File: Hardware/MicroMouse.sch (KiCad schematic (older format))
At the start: 70 parts, among them J1 TSW-106-25-S-S-RA, J3 PRPC040SFAN-RC (06), J4 B5B-XH-A(LF)(SN), J5 B5B-XH-A(LF)(SN), Q1 NXV75UPR, SW1 SPST, SW2 SPST, SW3 SPST, SW4 SPST, SW5 L101011MS02Q, SW6 SPST, SW7 SPST, SW8 SPST, U1 ADP1612, U2 PIC16F886-E_SO, U3 ULN2803ADW, U4 74LVC1G332GV-Q100H, U5 ADCMP393ARZ, U6 TCRT1000, U7 TCRT1000, U8 TCRT1000, Y1 32.768KHZ

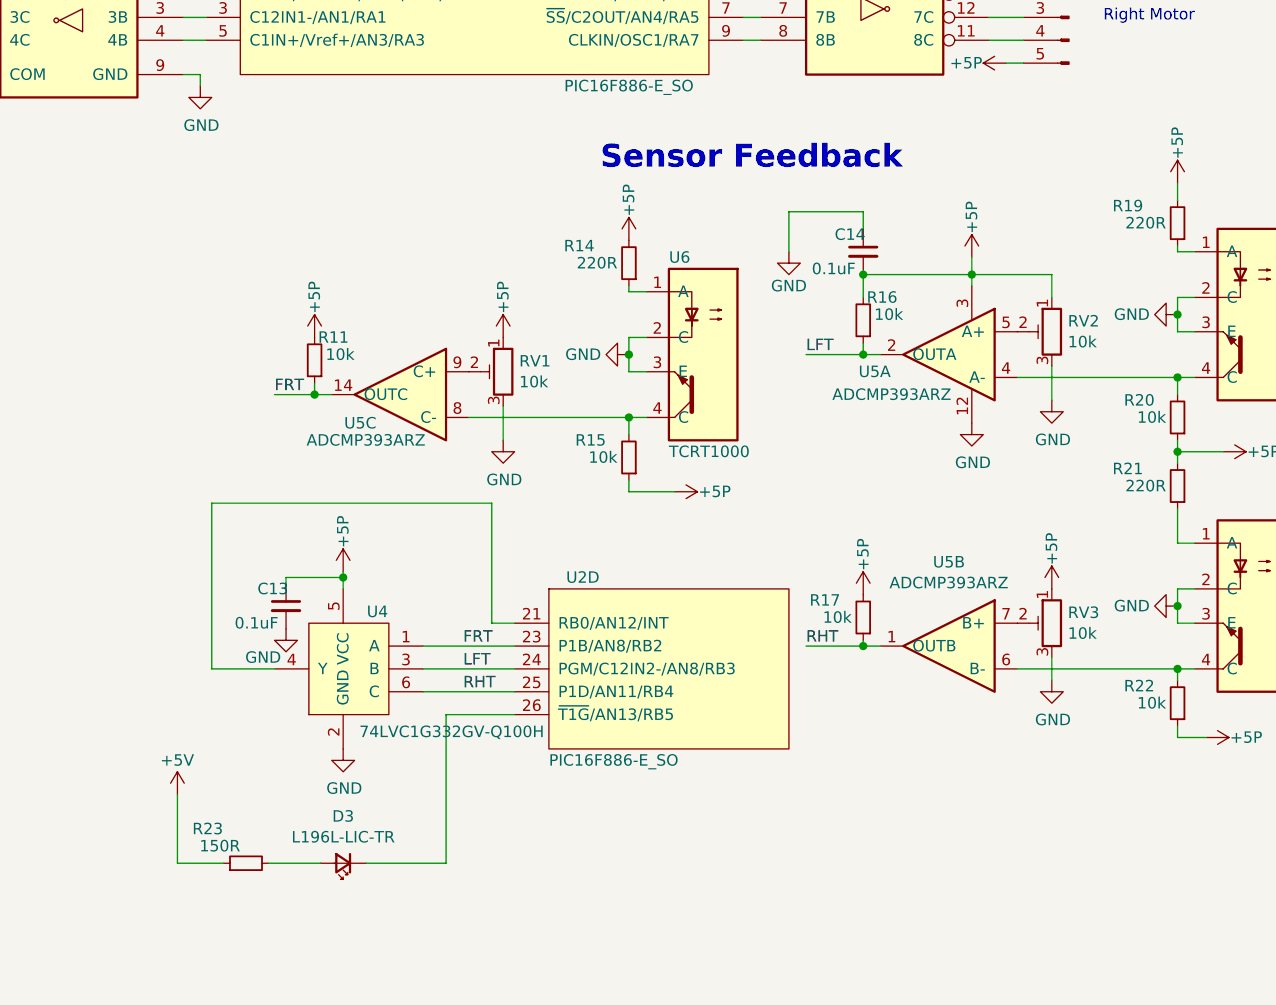
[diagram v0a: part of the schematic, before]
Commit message: Add LED for IR detection
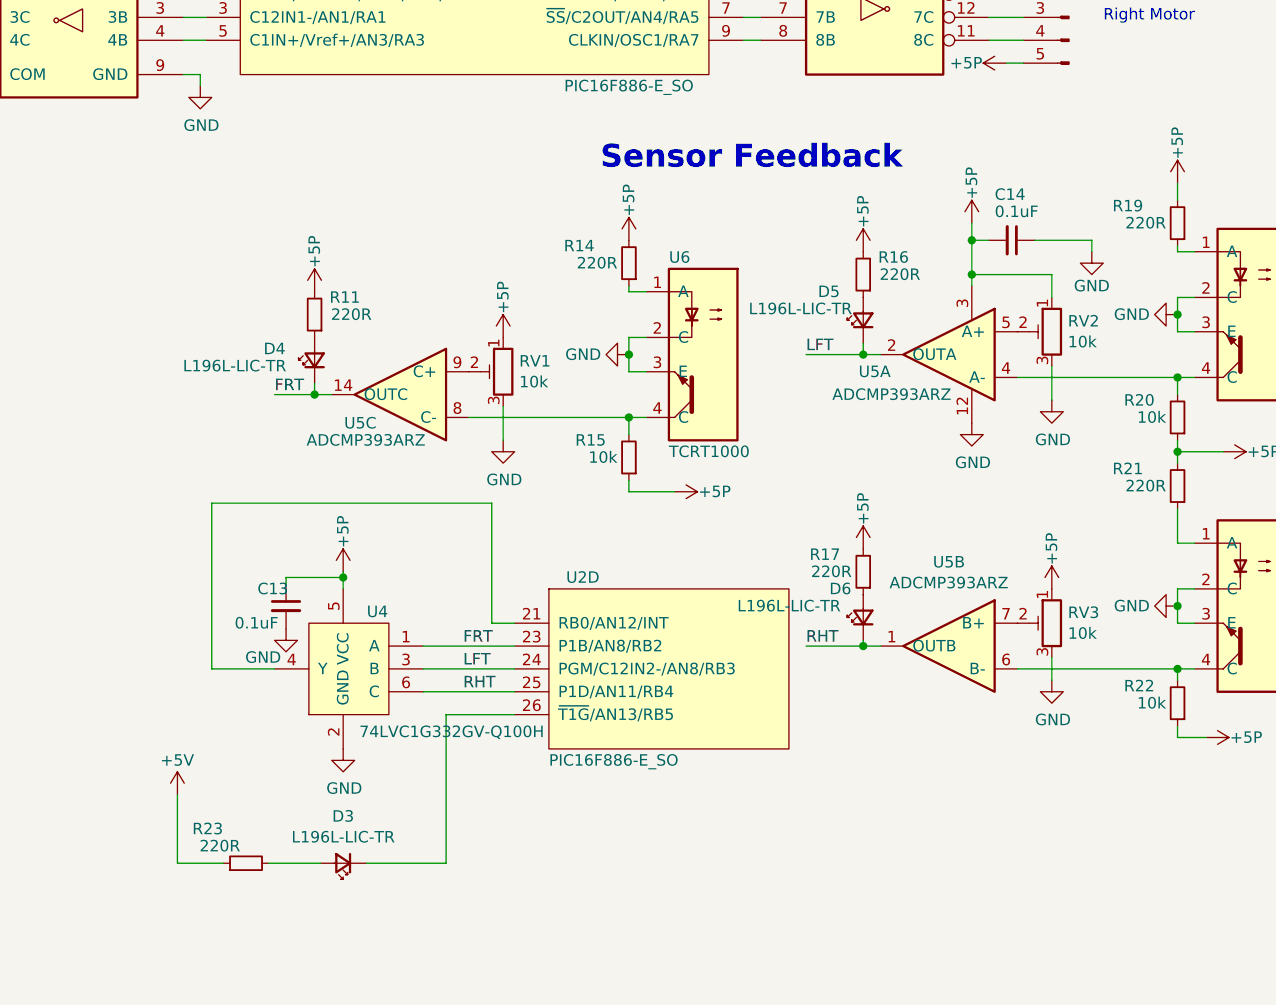
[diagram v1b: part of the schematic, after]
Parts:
- added D4, D5, D6: L196L-LIC-TR, Micro-Footprint:LTST-C170-0805, symbol Device:LED_Small
- R11, R16, R17: value 10k -> 220R
- R23: value 150R -> 220R
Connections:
- net FRT: now also D4.1 (K); no longer R11.1
- net LFT: now also D5.1 (K); no longer R16.1
- net RHT: now also D6.1 (K); no longer R17.1
- new net: D4.2 (A), R11.1
- new net: D5.2 (A), R16.1
- new net: D6.2 (A), R17.1
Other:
- moved on the sheet: C14, R11, R16, R17
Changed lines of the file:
@@
 EESchema Schematic File Version 4
-EELAYER 30 0
+LIBS:MicroMouse-cache
+EELAYER 29 0
 EELAYER END
 $Descr A4 11693 8268
@@
 Title "MicroMouse Mainboard with PIC16F886"
 Date "2021-04-11"
-Rev "1.00"
+Rev "1.10"
 Comp "KidoTech"
 Comment1 ""
@@
 L power:+5P #PWR037
 U 1 1 6090CAF6
-P 9200 4125
-F 0 "#PWR037" H 9200 3975 50  0001 C CNN
-F 1 "+5P" V 9200 4300 50  0000 C CNN
-F 2 "" H 9200 4125 50  0001 C CNN
-F 3 "" H 9200 4125 50  0001 C CNN
-	1    9200 4125
+P 9200 3975
+F 0 "#PWR037" H 9200 3825 50  0001 C CNN
+F 1 "+5P" V 9200 4150 50  0000 C CNN
+F 2 "" H 9200 3975 50  0001 C CNN
+F 3 "" H 9200 3975 50  0001 C CNN
+	1    9200 3975
 	1    0    0    -1
 $EndComp
@@
 L Device:R_Small R16
 U 1 1 60924A2D
-P 8725 4400
-F 0 "R16" H 8575 4300 50  0000 L CNN
-F 1 "10k" H 8550 4375 50  0000 L CNN
-F 2 "Micro-Footprint:RES0603" H 8725 4400 50  0001 C CNN
-F 3 "~" H 8725 4400 50  0001 C CNN
-	1    8725 4400
+P 8725 4200
+F 0 "R16" H 8525 4125 50  0000 L CNN
+F 1 "220R" H 8475 4200 50  0000 L CNN
+F 2 "Micro-Footprint:RES0603" H 8725 4200 50  0001 C CNN
+F 3 "~" H 8725 4200 50  0001 C CNN
+	1    8725 4200
 	-1   0    0    1
 $EndComp
@@
 Wire Wire Line
 	9200 4250 9200 4200
-Wire Wire Line
-	8725 4300 8725 4200
-Wire Wire Line
-	8725 4200 9200 4200
 Connection ~ 9200 4200
-Wire Wire Line
-	9200 4200 9200 4125
 $Comp
 L Device:C_Small C14
 U 1 1 60949563
-P 8725 4100
-F 0 "C14" H 8600 4175 50  0000 L CNN
-F 1 "0.1uF" H 8500 4025 50  0000 L CNN
-F 2 "Micro-Footprint:CAP0603" H 8725 4100 50  0001 C CNN
-F 3 "~" H 8725 4100 50  0001 C CNN
-	1    8725 4100
-	1    0    0    -1
+P 9375 4050
+F 0 "C14" V 9175 3975 50  0000 L CNN
+F 1 "0.1uF" V 9250 3975 50  0000 L CNN
+F 2 "Micro-Footprint:CAP0603" H 9375 4050 50  0001 C CNN
+F 3 "~" H 9375 4050 50  0001 C CNN
+	1    9375 4050
+	0    1    1    0
 $EndComp
 $Comp
 L power:GND #PWR035
 U 1 1 609636D6
-P 8400 4100
-F 0 "#PWR035" H 8400 3850 50  0001 C CNN
-F 1 "GND" H 8400 3950 50  0000 C CNN
-F 2 "" H 8400 4100 50  0001 C CNN
-F 3 "" H 8400 4100 50  0001 C CNN
-	1    8400 4100
+P 9725 4100
+F 0 "#PWR035" H 9725 3850 50  0001 C CNN
+F 1 "GND" H 9725 3950 50  0000 C CNN
+F 2 "" H 9725 4100 50  0001 C CNN
+F 3 "" H 9725 4100 50  0001 C CNN
+	1    9725 4100
 	1    0    0    -1
 $EndComp
@@
 L power:+5P #PWR036
 U 1 1 609B2C17
-P 8725 5600
-F 0 "#PWR036" H 8725 5450 50  0001 C CNN
-F 1 "+5P" V 8725 5775 50  0000 C CNN
-F 2 "" H 8725 5600 50  0001 C CNN
-F 3 "" H 8725 5600 50  0001 C CNN
-	1    8725 5600
+P 8725 5400
+F 0 "#PWR036" H 8725 5250 50  0001 C CNN
+F 1 "+5P" V 8725 5575 50  0000 C CNN
+F 2 "" H 8725 5400 50  0001 C CNN
+F 3 "" H 8725 5400 50  0001 C CNN
+	1    8725 5400
 	1    0    0    -1
 $EndComp
@@
 L Device:R_Small R17
 U 1 1 609A562F
-P 8725 5700
-F 0 "R17" H 8825 5625 50  0000 L CNN
-F 1 "10k" H 8775 5700 50  0000 L CNN
-F 2 "Micro-Footprint:RES0603" H 8725 5700 50  0001 C CNN
-F 3 "~" H 8725 5700 50  0001 C CNN
-	1    8725 5700
+P 8725 5500
+F 0 "R17" H 8825 5425 50  0000 L CNN
+F 1 "220R" H 8775 5500 50  0000 L CNN
+F 2 "Micro-Footprint:RES0603" H 8725 5500 50  0001 C CNN
+F 3 "~" H 8725 5500 50  0001 C CNN
+	1    8725 5500
 	-1   0    0    1
 $EndComp
@@
 L Device:R_Small R11
 U 1 1 609FA98A
-P 6325 4575
-F 0 "R11" H 6175 4475 50  0000 L CNN
-F 1 "10k" H 6150 4550 50  0000 L CNN
-F 2 "Micro-Footprint:RES0603" H 6325 4575 50  0001 C CNN
-F 3 "~" H 6325 4575 50  0001 C CNN
-	1    6325 4575
+P 6325 4375
+F 0 "R11" H 6125 4300 50  0000 L CNN
+F 1 "220R" H 6075 4375 50  0000 L CNN
+F 2 "Micro-Footprint:RES0603" H 6325 4375 50  0001 C CNN
+F 3 "~" H 6325 4375 50  0001 C CNN
+	1    6325 4375
 	-1   0    0    1
 $EndComp
@@
 L power:+5P #PWR025
 U 1 1 60AB88D8
-P 6325 4475
-F 0 "#PWR025" H 6325 4325 50  0001 C CNN
-F 1 "+5P" V 6325 4650 50  0000 C CNN
-F 2 "" H 6325 4475 50  0001 C CNN
-F 3 "" H 6325 4475 50  0001 C CNN
-	1    6325 4475
+P 6325 4275
+F 0 "#PWR025" H 6325 4125 50  0001 C CNN
+F 1 "+5P" V 6325 4450 50  0000 C CNN
+F 2 "" H 6325 4275 50  0001 C CNN
+F 3 "" H 6325 4275 50  0001 C CNN
+	1    6325 4275
 	1    0    0    -1
 $EndComp
@@
 	8725 4550 8475 4550
 Connection ~ 8725 4550
-Connection ~ 8725 4200
-Wire Wire Line
-	8400 4100 8400 3925
-Wire Wire Line
-	8400 3925 8725 3925
-Wire Wire Line
-	8725 3925 8725 4000
 Text Label 8475 5825 0    50   ~ 0
 RHT
@@
 P 6025 6775
 F 0 "R23" V 6175 6875 50  0000 L CNN
-F 1 "150R" V 6100 6800 50  0000 L CNN
+F 1 "220R" V 6100 6800 50  0000 L CNN
 F 2 "Micro-Footprint:RES0603" H 6025 6775 50  0001 C CNN
 F 3 "~" H 6025 6775 50  0001 C CNN
@@
 Text Label 4025 7000 0    50   ~ 0
 C3
+$Comp
+L Device:LED_Small D4
+U 1 1 6073DD47
+P 6325 4575
+F 0 "D4" V 6375 4750 50  0000 C CNN
+F 1 "L196L-LIC-TR" V 6300 4925 50  0000 C CNN
+F 2 "Micro-Footprint:LTST-C170-0805" V 6325 4575 50  0001 C CNN
+F 3 "~" V 6325 4575 50  0001 C CNN
+	1    6325 4575
+	0    -1   -1   0
+$EndComp
+$Comp
+L Device:LED_Small D5
+U 1 1 6073EA1A
+P 8725 4400
+F 0 "D5" V 8850 4550 50  0000 C CNN
+F 1 "L196L-LIC-TR" V 8775 4675 50  0000 C CNN
+F 2 "Micro-Footprint:LTST-C170-0805" V 8725 4400 50  0001 C CNN
+F 3 "~" V 8725 4400 50  0001 C CNN
+	1    8725 4400
+	0    -1   -1   0
+$EndComp
+$Comp
+L Device:LED_Small D6
+U 1 1 6073EDC0
+P 8725 5700
+F 0 "D6" V 8850 5800 50  0000 C CNN
+F 1 "L196L-LIC-TR" V 8775 6025 50  0000 C CNN
+F 2 "Micro-Footprint:LTST-C170-0805" V 8725 5700 50  0001 C CNN
+F 3 "~" V 8725 5700 50  0001 C CNN
+	1    8725 5700
+	0    -1   -1   0
+$EndComp
+Wire Wire Line
+	9200 3975 9200 4050
+Wire Wire Line
+	9275 4050 9200 4050
+Connection ~ 9200 4050
+Wire Wire Line
+	9200 4050 9200 4200
+Wire Wire Line
+	9475 4050 9725 4050
+Wire Wire Line
+	9725 4050 9725 4100
+$Comp
+L power:+5P #PWR049
+U 1 1 607CD14E
+P 8725 4100
+F 0 "#PWR049" H 8725 3950 50  0001 C CNN
+F 1 "+5P" V 8725 4275 50  0000 C CNN
+F 2 "" H 8725 4100 50  0001 C CNN
+F 3 "" H 8725 4100 50  0001 C CNN
+	1    8725 4100
+	1    0    0    -1
+$EndComp
 $EndSCHEMATC

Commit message: Update Layout
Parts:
- removed BT1: 1042, Micro-Footprint:1042-SMD, symbol Device:Battery_Cell
- removed J3: PRPC040SFAN-RC (06), Micro-Footprint:THRU-254-STR-6P, symbol Connector:Conn_01x06_Male
- removed SW5: L101011MS02Q, Micro-Footprint:L101011-THRU, symbol Switch:SW_DIP_x01
- added J2: B2B-PH-K-S(LF)(SN), Micro-Footprint:THRU-200-STR-2P, symbol Connector:Conn_01x02_Male
- added J3: Conn_01x04_Male, Micro-Footprint:THRU-254-STR-4P, symbol Connector:Conn_01x04_Male
- added R24, R25: 1k, Micro-Footprint:RES0603, symbol Device:R_Small
- U6, U7, U8: footprint Micro-Footprint:LTST-C170-0805 -> Micro-Footprint:TCRT1000-THRU
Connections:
- net +5P: now also J1.2 (Pin_2), R12.2, R23.1, R7.2, R8.2, U2.20 (VDD), J3.2 (Pin_2), R24.2, R25.2; no longer C7.1, C8.1, J4.5 (Pin_5), J5.5 (Pin_5), U3.10 (COM)
- net +5V: now also C7.1, C8.1, J4.5 (Pin_5), J5.5 (Pin_5), U3.10 (COM); no longer J1.2 (Pin_2), R12.2, R23.1, R7.2, R8.2, U2.20 (VDD)
- net GND: now also J2.2 (Pin_2), J3.1 (Pin_1)
- net at Q1.3 (D): now also J2.1 (Pin_1)
- net at U2.14 (RC3/SCK/SCL): now also J3.3 (Pin_3), R25.1
- net at U2.15 (RC4/SDI/SDA): now also J3.4 (Pin_4), R24.1
- net C1 renamed CL1
- net C2 renamed CL2
- net C3 renamed CL3
- net R1 renamed RW1
- net R2 renamed RW2
- no-connect marks 0 -> 4
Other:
- moved on the sheet: C7, C8

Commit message: Layout
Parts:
- removed C11: 1uF, Micro-Footprint:CAP0603, symbol Device:C_Small
- C9: value 1uF -> 0.1uF
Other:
- moved on the sheet: C12
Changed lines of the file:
@@
 	10025 1875 10025 1950
-$Comp
-L Device:C_Small C11
-U 1 1 607C5E25
-P 5725 1275
-F 0 "C11" H 5550 1350 50  0000 L CNN
-F 1 "1uF" H 5550 1200 50  0000 L CNN
-F 2 "Micro-Footprint:CAP0603" H 5725 1275 50  0001 C CNN
-F 3 "~" H 5725 1275 50  0001 C CNN
-	1    5725 1275
-	1    0    0    -1
-$EndComp
 $Comp
 L Device:C_Small C12
 U 1 1 607C6AE3
-P 5900 1275
-F 0 "C12" H 5950 1350 50  0000 L CNN
-F 1 "0.1uF" H 5950 1200 50  0000 L CNN
-F 2 "Micro-Footprint:CAP0603" H 5900 1275 50  0001 C CNN
-F 3 "~" H 5900 1275 50  0001 C CNN
-	1    5900 1275
+P 5725 1150
+F 0 "C12" H 5775 1225 50  0000 L CNN
+F 1 "0.1uF" H 5775 1075 50  0000 L CNN
+F 2 "Micro-Footprint:CAP0603" H 5725 1150 50  0001 C CNN
+F 3 "~" H 5725 1150 50  0001 C CNN
+	1    5725 1150
 	1    0    0    -1
 $EndComp
@@
 	1    0    0    -1
 $EndComp
-Wire Wire Line
-	5725 1175 5725 1125
-Wire Wire Line
-	5900 1175 5900 1125
-Wire Wire Line
-	5900 1125 5725 1125
-Connection ~ 5725 1125
-Wire Wire Line
-	5725 1125 5725 1050
 $Comp
 L power:GND #PWR021
 U 1 1 607CD1DE
-P 5725 1525
-F 0 "#PWR021" H 5725 1275 50  0001 C CNN
-F 1 "GND" H 5730 1352 50  0000 C CNN
-F 2 "" H 5725 1525 50  0001 C CNN
-F 3 "" H 5725 1525 50  0001 C CNN
-	1    5725 1525
+P 5725 1250
+F 0 "#PWR021" H 5725 1000 50  0001 C CNN
+F 1 "GND" H 5730 1077 50  0000 C CNN
+F 2 "" H 5725 1250 50  0001 C CNN
+F 3 "" H 5725 1250 50  0001 C CNN
+	1    5725 1250
 	1    0    0    -1
 $EndComp
@@
 	9350 3275 9400 3275
 $Comp
-L Device:C_Small C9
-U 1 1 607C4D9D
-P 5100 1325
-F 0 "C9" H 4925 1400 50  0000 L CNN
-F 1 "1uF" H 4925 1250 50  0000 L CNN
-F 2 "Micro-Footprint:CAP0603" H 5100 1325 50  0001 C CNN
-F 3 "~" H 5100 1325 50  0001 C CNN
-	1    5100 1325
-	1    0    0    -1
-$EndComp
-$Comp
 L Device:C_Small C10
 U 1 1 607C5B06
 P 5325 1325
-F 0 "C10" H 5150 1400 50  0000 L CNN
-F 1 "1uF" H 5150 1250 50  0000 L CNN
+F 0 "C10" H 5400 1350 50  0000 L CNN
+F 1 "1uF" H 5400 1275 50  0000 L CNN
 F 2 "Micro-Footprint:CAP0603" H 5325 1325 50  0001 C CNN
 F 3 "~" H 5325 1325 50  0001 C CNN
@@
 Wire Wire Line
 	6450 5525 6450 5500
-Wire Wire Line
-	5725 1525 5725 1450
-Wire Wire Line
-	5900 1375 5900 1450
-Wire Wire Line
-	5900 1450 5725 1450
-Connection ~ 5725 1450
-Wire Wire Line
-	5725 1450 5725 1375
 Wire Wire Line
 	1650 6275 1650 6225
@@
 	3275 2250 3275 2225
 $Comp
-L power:GND #PWR?
+L power:GND #PWR0108
 U 1 1 6137EB99
 P 4500 3750
-F 0 "#PWR?" H 4500 3500 50  0001 C CNN
+F 0 "#PWR0108" H 4500 3500 50  0001 C CNN
 F 1 "GND" H 4505 3577 50  0000 C CNN
 F 2 "" H 4500 3750 50  0001 C CNN
@@
 	4500 3750 4500 3600
 $Comp
-L power:GND #PWR?
+L power:GND #PWR0109
 U 1 1 613AB2FA
 P 9400 3575
-F 0 "#PWR?" H 9400 3325 50  0001 C CNN
+F 0 "#PWR0109" H 9400 3325 50  0001 C CNN
 F 1 "GND" H 9400 3425 50  0000 C CNN
 F 2 "" H 9400 3575 50  0001 C CNN
@@
 Wire Wire Line
 	9400 3575 9400 3525
+$Comp
+L Device:C_Small C9
+U 1 1 60D66234
+P 5100 1325
+F 0 "C9" H 4900 1350 50  0000 L CNN
+F 1 "0.1uF" H 4875 1250 50  0000 L CNN
+F 2 "Micro-Footprint:CAP0603" H 5100 1325 50  0001 C CNN
+F 3 "~" H 5100 1325 50  0001 C CNN
+	1    5100 1325
+	1    0    0    -1
+$EndComp
 $EndSCHEMATC

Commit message: Update layout
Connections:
- no-connect marks 4 -> 2
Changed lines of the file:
@@
 EESchema Schematic File Version 4
-LIBS:MicroMouse-cache
-EELAYER 29 0
+EELAYER 30 0
 EELAYER END
 $Descr A4 11693 8268
@@
 NoConn ~ 3250 5025
 NoConn ~ 3250 5525
-NoConn ~ 975  600
-NoConn ~ 675  1750
 $Comp
 L power:+5P #PWR0101
